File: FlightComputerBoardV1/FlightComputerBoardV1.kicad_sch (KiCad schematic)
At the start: 0 parts

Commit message: Added PT_RELAY schematic
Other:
- added sheet PT_RELAY (PT_RELAY.kicad_sch)
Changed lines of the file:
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@@
 	(generator_version "10.0")
 	(paper "A4")
+	(sheet
+		(at 81.28 104.14)
+		(size 45.72 33.02)
+		(exclude_from_sim no)
+		(in_bom yes)
+		(on_board yes)
+		(dnp no)
+		(fields_autoplaced yes)
+		(stroke
+			(width 0.1524)
+			(type solid)
+		)
+		(fill
+			(color 0 0 0 0)
+		)
+		(property "Sheetname" "PT_RELAY"
+			(at 81.28 103.4284 0)
+			(show_name no)
+			(do_not_autoplace no)
+			(effects
+				(font
+					(size 1.27 1.27)
+				)
+				(justify left bottom)
+			)
+		)
+		(property "Sheetfile" "PT_RELAY.kicad_sch"
+			(at 81.28 137.7446 0)
+			(show_name no)
+			(do_not_autoplace no)
+			(effects
+				(font
+					(size 1.27 1.27)
+				)
+				(justify left top)
+			)
+		)
+		(instances
+			(project "FlightComputerBoardV1"
+				(path "/7795ce7a-d456-4fa5-b86a-75a229c2d679"
+					(page "2")
+				)
+			)
+		)
+	)
 	(sheet_instances
 		(path "/"

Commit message: Added sheets and hierarchy labels
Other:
- added sheet MCU (MCU.kicad_sch)
- sheet PT_RELAY ports: added PT1, PT2, PT3, PT4, PT5, PT6, PT7, PT8, PT9; removed none
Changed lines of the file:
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@@
 	(paper "A4")
 	(sheet
-		(at 81.28 104.14)
+		(at 72.39 113.03)
 		(size 45.72 33.02)
 		(exclude_from_sim no)
@@
 		)
 		(property "Sheetname" "PT_RELAY"
-			(at 81.28 103.4284 0)
+			(at 72.39 112.3184 0)
 			(show_name no)
 			(do_not_autoplace no)
@@
 		)
 		(property "Sheetfile" "PT_RELAY.kicad_sch"
-			(at 81.28 137.7446 0)
+			(at 72.39 146.6346 0)
+			(show_name no)
+			(do_not_autoplace no)
+			(effects
+				(font
+					(size 1.27 1.27)
+				)
+				(justify left top)
+			)
+		)
+		(pin "PT1" output
+			(at 85.09 113.03 90)
+			(effects
+				(font
+					(size 1.27 1.27)
+				)
+				(justify right)
+			)
+		)
+		(pin "PT2" output
+			(at 91.44 113.03 90)
+			(effects
+				(font
+					(size 1.27 1.27)
+				)
+				(justify right)
+			)
+		)
+		(pin "PT3" output
+			(at 97.79 113.03 90)
+			(effects
+				(font
+					(size 1.27 1.27)
+				)
+				(justify right)
+			)
+		)
+		(pin "PT4" output
+			(at 104.14 113.03 90)
+			(effects
+				(font
+					(size 1.27 1.27)
+				)
+				(justify right)
+			)
+		)
+		(pin "PT5" output
+			(at 110.49 113.03 90)
+			(effects
+				(font
+					(size 1.27 1.27)
+				)
+				(justify right)
+			)
+		)
+		(pin "PT6" output
+			(at 118.11 120.65 0)
+			(effects
+				(font
+					(size 1.27 1.27)
+				)
+				(justify right)
+			)
+		)
+		(pin "PT7" output
+			(at 118.11 127 0)
+			(effects
+				(font
+					(size 1.27 1.27)
+				)
+				(justify right)
+			)
+		)
+		(pin "PT8" output
+			(at 118.11 133.35 0)
+			(effects
+				(font
+					(size 1.27 1.27)
+				)
+				(justify right)
+			)
+		)
+		(pin "PT9" output
+			(at 118.11 139.7 0)
+			(effects
+				(font
+					(size 1.27 1.27)
+				)
+				(justify right)
+			)
+		)
+		(instances
+			(project "FlightComputerBoardV1"
+				(path "/7795ce7a-d456-4fa5-b86a-75a229c2d679"
+					(page "2")
+				)
+			)
+		)
+	)
+	(sheet
+		(at 130.81 60.96)
+		(size 49.53 34.29)
+		(exclude_from_sim no)
+		(in_bom yes)
+		(on_board yes)
+		(dnp no)
+		(fields_autoplaced yes)
+		(stroke
+			(width 0.1524)
+			(type solid)
+		)
+		(fill
+			(color 0 0 0 0)
+		)
+		(property "Sheetname" "MCU"
+			(at 130.81 60.2484 0)
+			(show_name no)
+			(do_not_autoplace no)
+			(effects
+				(font
+					(size 1.27 1.27)
+				)
+				(justify left bottom)
+			)
+		)
+		(property "Sheetfile" "MCU.kicad_sch"
+			(at 130.81 95.8346 0)
 			(show_name no)
 			(do_not_autoplace no)
@@
 			(project "FlightComputerBoardV1"
 				(path "/7795ce7a-d456-4fa5-b86a-75a229c2d679"
-					(page "2")
+					(page "3")
 				)
 			)

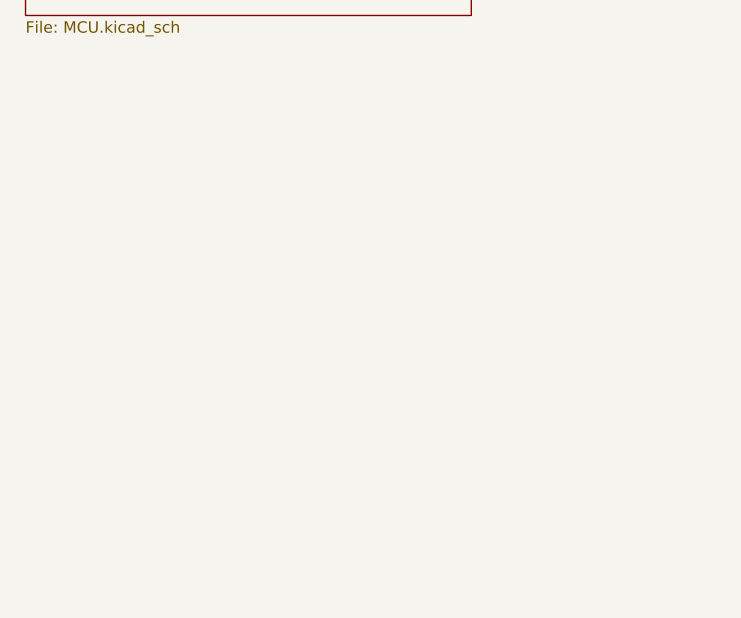
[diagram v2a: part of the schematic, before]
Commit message: added power hierarchy
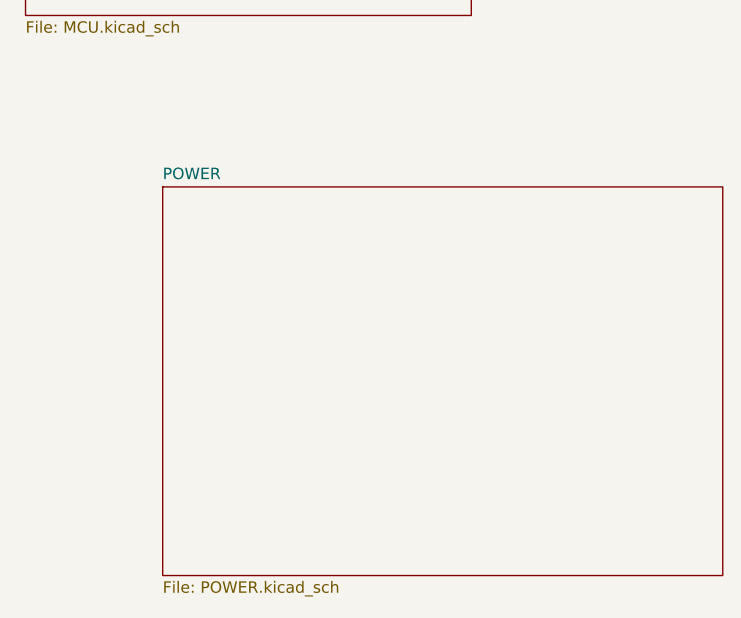
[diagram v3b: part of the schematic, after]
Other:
- added sheet POWER (POWER.kicad_sch)
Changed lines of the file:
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@@
+		)
+	)
+	(sheet
+		(at 146.05 114.3)
+		(size 62.23 43.18)
+		(exclude_from_sim no)
+		(in_bom yes)
+		(on_board yes)
+		(dnp no)
+		(fields_autoplaced yes)
+		(stroke
+			(width 0.1524)
+			(type solid)
+		)
+		(fill
+			(color 0 0 0 0)
+		)
+		(property "Sheetname" "POWER"
+			(at 146.05 113.5884 0)
+			(show_name no)
+			(do_not_autoplace no)
+			(effects
+				(font
+					(size 1.27 1.27)
+				)
+				(justify left bottom)
+			)
+		)
+		(property "Sheetfile" "POWER.kicad_sch"
+			(at 146.05 158.0646 0)
+			(show_name no)
+			(do_not_autoplace no)
+			(effects
+				(font
+					(size 1.27 1.27)
+				)
+				(justify left top)
+			)
+		)
+		(instances
+			(project "FlightComputerBoardV1"
+				(path "/7795ce7a-d456-4fa5-b86a-75a229c2d679"
+					(page "4")
+				)
+			)
 		)
 	)

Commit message: Added imu to peripherals sheet
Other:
- added sheet Peripherals (Peripherals.kicad_sch)
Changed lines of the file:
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@@
+	)
+	(sheet
+		(at 48.26 38.1)
+		(size 44.45 31.75)
+		(exclude_from_sim no)
+		(in_bom yes)
+		(on_board yes)
+		(dnp no)
+		(fields_autoplaced yes)
+		(stroke
+			(width 0.1524)
+			(type solid)
+		)
+		(fill
+			(color 0 0 0 0)
+		)
+		(property "Sheetname" "Peripherals"
+			(at 48.26 37.3884 0)
+			(show_name no)
+			(do_not_autoplace no)
+			(effects
+				(font
+					(size 1.27 1.27)
+				)
+				(justify left bottom)
+			)
+		)
+		(property "Sheetfile" "Peripherals.kicad_sch"
+			(at 48.26 70.4346 0)
+			(show_name no)
+			(do_not_autoplace no)
+			(effects
+				(font
+					(size 1.27 1.27)
+				)
+				(justify left top)
+			)
+		)
+		(pin "SCL_I2C_X" bidirectional
+			(at 92.71 46.99 0)
+			(effects
+				(font
+					(size 1.27 1.27)
+				)
+				(justify right)
+			)
+		)
+		(pin "SDA_I2C_X" bidirectional
+			(at 92.71 52.07 0)
+			(effects
+				(font
+					(size 1.27 1.27)
+				)
+				(justify right)
+			)
+		)
+		(instances
+			(project "FlightComputerBoardV1"
+				(path "/7795ce7a-d456-4fa5-b86a-75a229c2d679"
+					(page "5")
+				)
+			)
+		)
 	)
 	(sheet

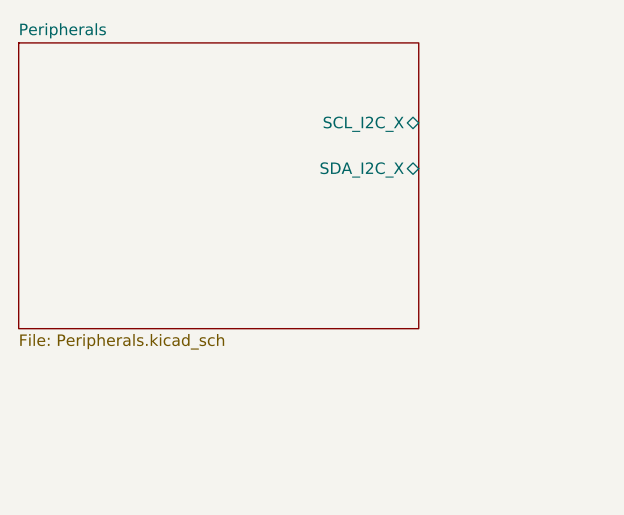
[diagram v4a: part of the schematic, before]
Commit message: Finished peripherals-IMU schematic sheet
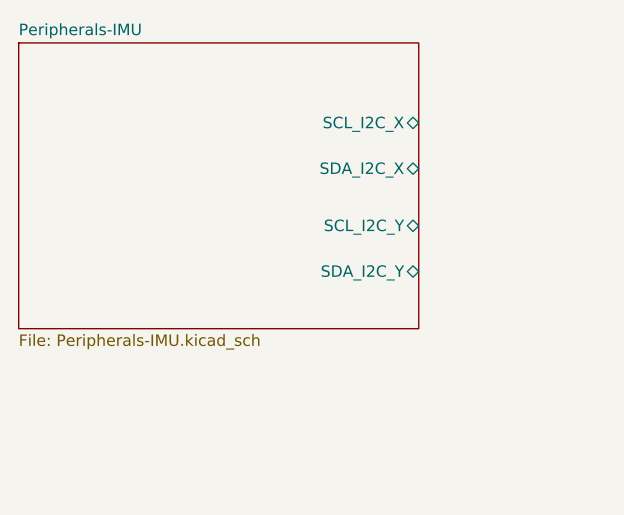
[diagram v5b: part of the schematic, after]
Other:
- sheet Peripherals renamed Peripherals-IMU
- sheet Peripherals-IMU: file Peripherals.kicad_sch -> Peripherals-IMU.kicad_sch
- sheet Peripherals-IMU ports: added SCL_I2C_Y, SDA_I2C_Y; removed none
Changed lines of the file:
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@@
 			(color 0 0 0 0)
 		)
-		(property "Sheetname" "Peripherals"
+		(property "Sheetname" "Peripherals-IMU"
 			(at 48.26 37.3884 0)
 			(show_name no)
@@
 			)
 		)
-		(property "Sheetfile" "Peripherals.kicad_sch"
+		(property "Sheetfile" "Peripherals-IMU.kicad_sch"
 			(at 48.26 70.4346 0)
 			(show_name no)
@@
 			(effects
 				(font
+					(size 1.27 1.27)
+				)
+				(justify right)
+			)
+		)
+		(pin "SCL_I2C_Y" bidirectional
+			(at 92.71 58.42 0)
+			(effects
+				(font
+					(size 1.27 1.27)
+				)
+				(justify right)
+			)
+		)
+		(pin "SDA_I2C_Y" bidirectional
+			(at 92.71 63.5 0)
+			(effects
+				(font

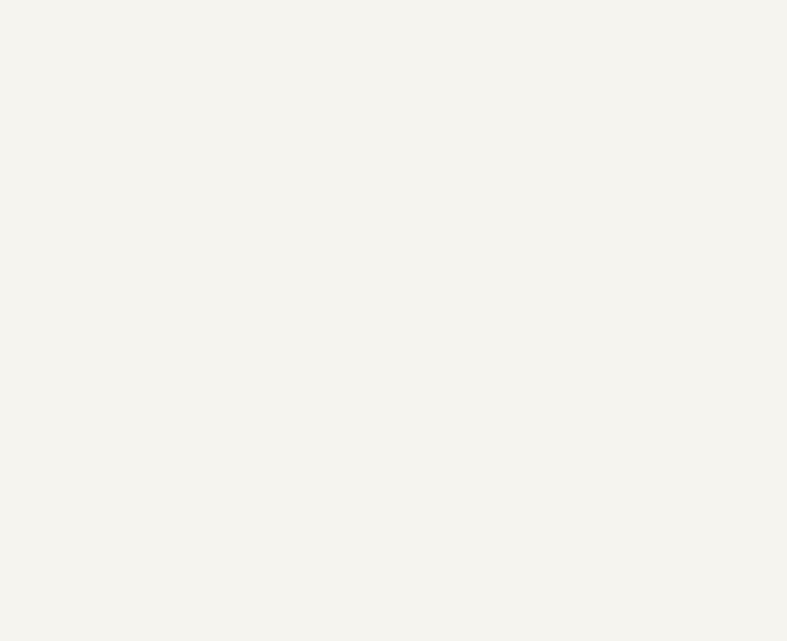
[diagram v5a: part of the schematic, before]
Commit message: Added GPS
- Added GPS schematic
- Added GPS symbol
- Added GPS footprint
- Created connections for I2C to root schematic page for GPS
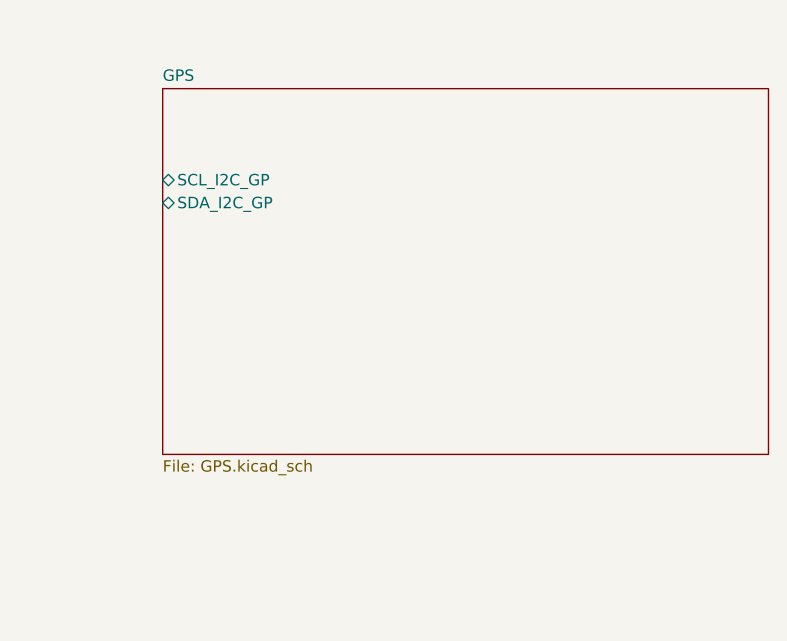
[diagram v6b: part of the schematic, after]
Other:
- added sheet GPS (GPS.kicad_sch)
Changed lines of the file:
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@@
+		)
+	)
+	(sheet
+		(at 199.39 43.18)
+		(size 67.31 40.64)
+		(exclude_from_sim no)
+		(in_bom yes)
+		(on_board yes)
+		(dnp no)
+		(fields_autoplaced yes)
+		(stroke
+			(width 0.1524)
+			(type solid)
+		)
+		(fill
+			(color 0 0 0 0)
+		)
+		(property "Sheetname" "GPS"
+			(at 199.39 42.4684 0)
+			(show_name no)
+			(do_not_autoplace no)
+			(effects
+				(font
+					(size 1.27 1.27)
+				)
+				(justify left bottom)
+			)
+		)
+		(property "Sheetfile" "GPS.kicad_sch"
+			(at 199.39 84.4046 0)
+			(show_name no)
+			(do_not_autoplace no)
+			(effects
+				(font
+					(size 1.27 1.27)
+				)
+				(justify left top)
+			)
+		)
+		(pin "SCL_I2C_GP" bidirectional
+			(at 199.39 53.34 180)
+			(effects
+				(font
+					(size 1.27 1.27)
+				)
+				(justify left)
+			)
+		)
+		(pin "SDA_I2C_GP" bidirectional
+			(at 199.39 55.88 180)
+			(effects
+				(font
+					(size 1.27 1.27)
+				)
+				(justify left)
+			)
+		)
+		(instances
+			(project "FlightComputerBoardV1"
+				(path "/7795ce7a-d456-4fa5-b86a-75a229c2d679"
+					(page "6")
+				)
+			)
 		)
 	)

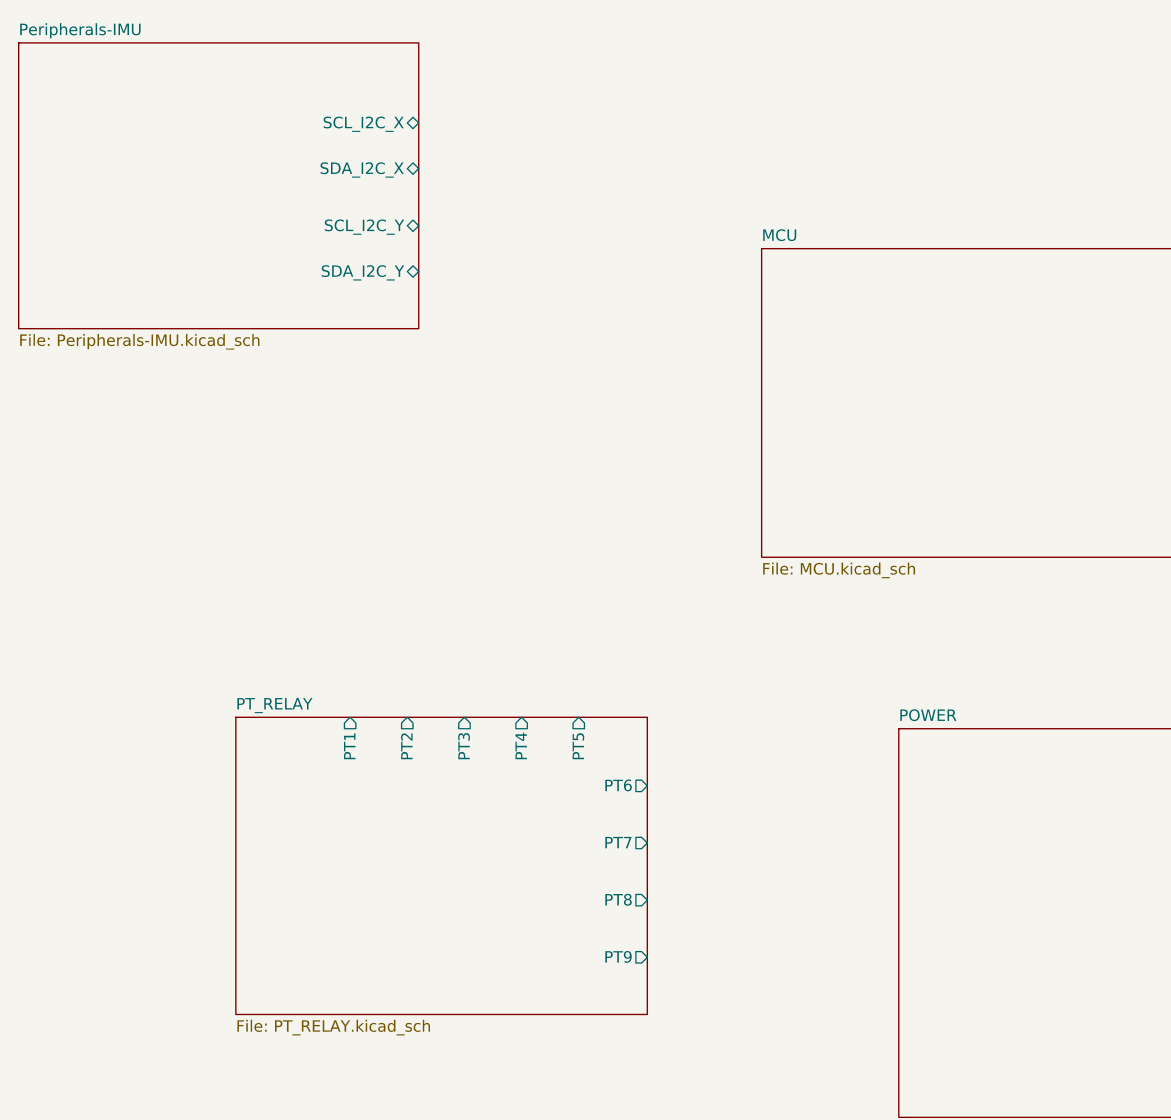
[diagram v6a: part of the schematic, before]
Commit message: Test Points, BMP581
- Added I2C and other test points to schematic
- Added BMP581 symbol, footprint, and schematic on Peripherals sheet
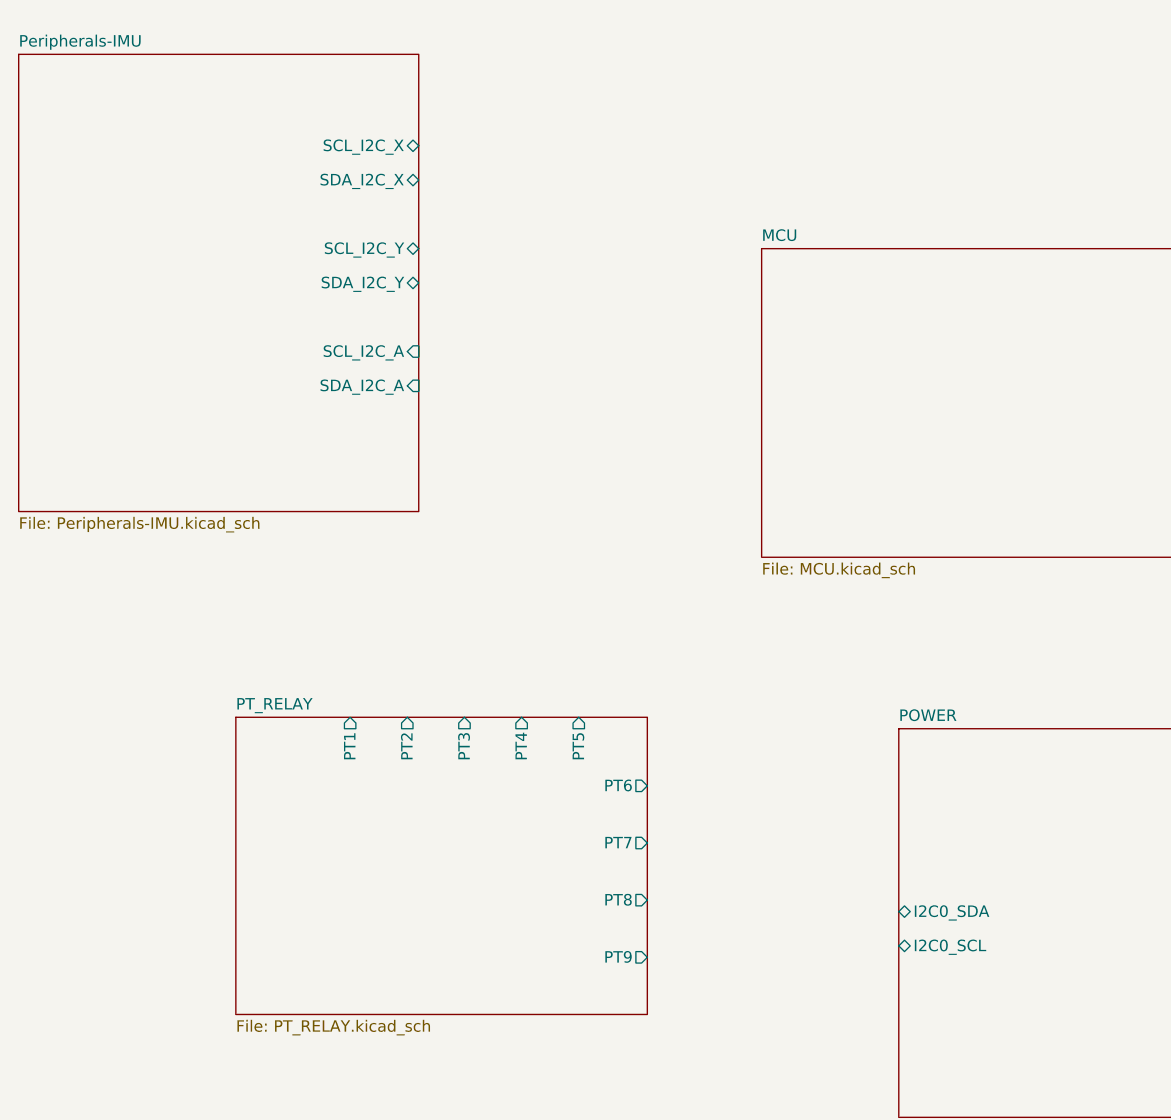
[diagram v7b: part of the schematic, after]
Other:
- sheet POWER ports: added I2C0_SCL, I2C0_SDA; removed none
- sheet Peripherals-IMU ports: added SCL_I2C_A, SDA_I2C_A; removed none
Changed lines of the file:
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@@
 	)
 	(sheet
-		(at 48.26 38.1)
-		(size 44.45 31.75)
+		(at 48.26 39.37)
+		(size 44.45 50.8)
 		(exclude_from_sim no)
 		(in_bom yes)
@@
 		)
 		(property "Sheetname" "Peripherals-IMU"
-			(at 48.26 37.3884 0)
+			(at 48.26 38.6584 0)
 			(show_name no)
 			(do_not_autoplace no)
@@
 		)
 		(property "Sheetfile" "Peripherals-IMU.kicad_sch"
-			(at 48.26 70.4346 0)
+			(at 48.26 90.7546 0)
 			(show_name no)
 			(do_not_autoplace no)
@@
 		)
 		(pin "SCL_I2C_X" bidirectional
-			(at 92.71 46.99 0)
+			(at 92.71 49.53 0)
 			(effects
 				(font
@@
 		)
 		(pin "SDA_I2C_X" bidirectional
-			(at 92.71 52.07 0)
+			(at 92.71 53.34 0)
 			(effects
 				(font
@@
 		)
 		(pin "SCL_I2C_Y" bidirectional
-			(at 92.71 58.42 0)
+			(at 92.71 60.96 0)
 			(effects
 				(font
@@
 		)
 		(pin "SDA_I2C_Y" bidirectional
-			(at 92.71 63.5 0)
+			(at 92.71 64.77 0)
+			(effects
+				(font
+					(size 1.27 1.27)
+				)
+				(justify right)
+			)
+		)
+		(pin "SCL_I2C_A" input
+			(at 92.71 72.39 0)
+			(effects
+				(font
+					(size 1.27 1.27)
+				)
+				(justify right)
+			)
+		)
+		(pin "SDA_I2C_A" input
+			(at 92.71 76.2 0)
 			(effects
 				(font
@@
 			)
 		)
+		(pin "I2C0_SCL" bidirectional
+			(at 146.05 138.43 180)
+			(effects
+				(font
+					(size 1.27 1.27)
+				)
+				(justify left)
+			)
+		)
+		(pin "I2C0_SDA" bidirectional
+			(at 146.05 134.62 180)
+			(effects
+				(font
+					(size 1.27 1.27)
+				)
+				(justify left)
+			)
+		)
